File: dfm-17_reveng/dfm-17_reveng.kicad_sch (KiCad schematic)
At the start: 40 parts, among them T1 Thermistor_PTC, T2 Thermistor_PTC, U1 ADG719, U2 ADG719, U3 ADG719, U4 ADG719

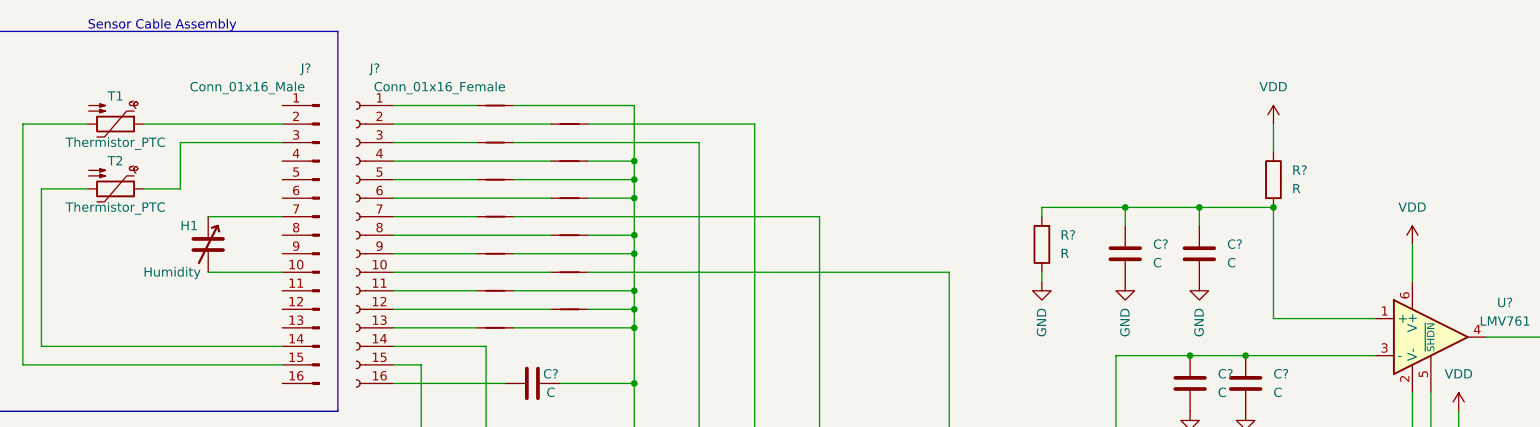
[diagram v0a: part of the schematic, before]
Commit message: small schematic comments, add pics
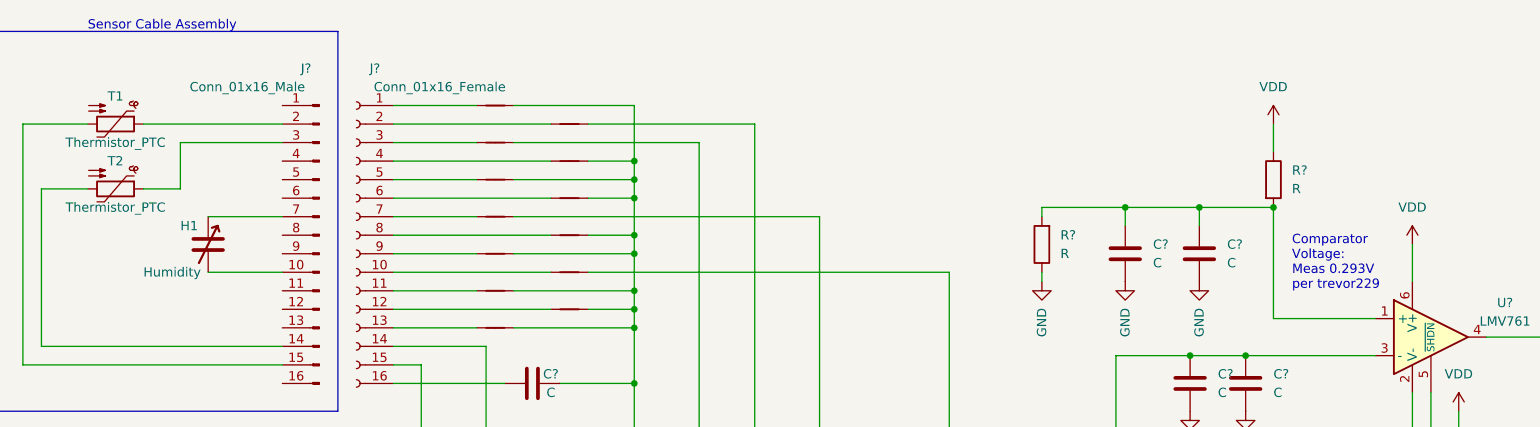
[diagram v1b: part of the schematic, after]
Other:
- note added: "Comparator Voltage: Meas 0.293V per trevor229"
